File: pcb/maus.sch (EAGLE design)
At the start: 84 parts, among them IC1 AD712R, Q2 BSS123, Q3 BSL307SP, Q4 BSS123, T1 BC847, T2 BC847, U1 ESP32-S2-WROOM, U2 CH340C, U3 CP2102, U4 LP3965EMP-3.3, U5 LSM9DS1TR

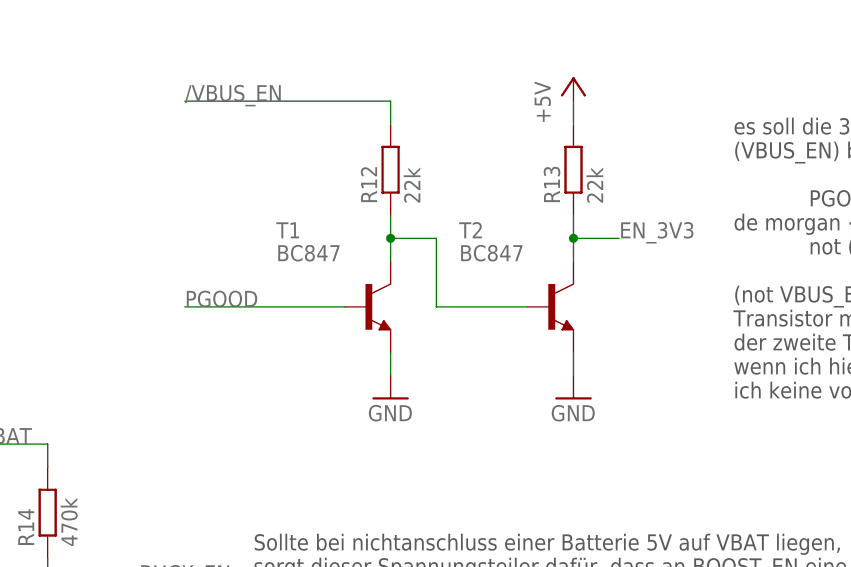
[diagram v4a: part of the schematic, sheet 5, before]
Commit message: swapped BC847 -> BSS123 in power schematics
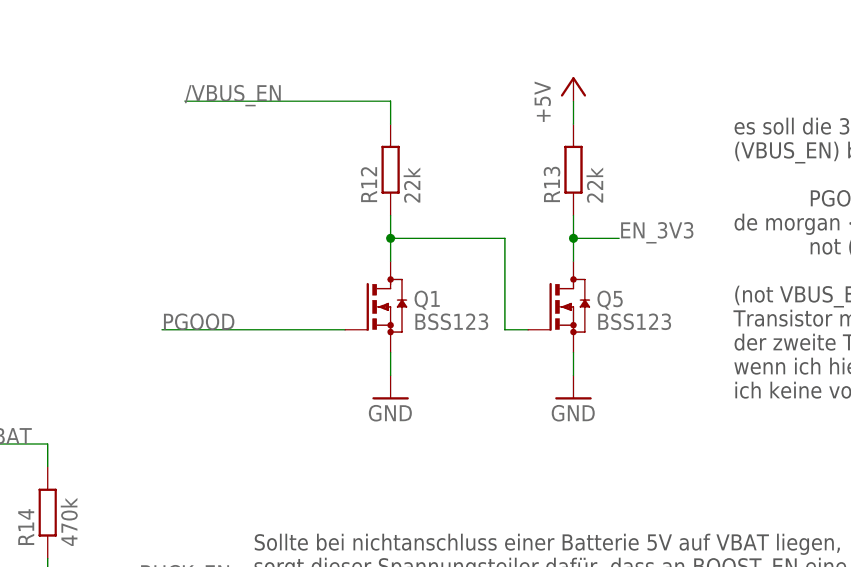
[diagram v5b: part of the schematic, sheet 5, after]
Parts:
- removed T1, T2: BC847, transistor:BC847
- added Q1, Q5: BSS123, transistor-small-signal:BSS123
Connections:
- net EN_3V3: now also Q5.D; no longer T2.C
- net GND: now also Q1.S, Q5.S; no longer T1.E, T2.E
- net N$20: now also Q1.D, Q5.G; no longer T1.C, T2.B
- net PGOOD: now also Q1.G; no longer T1.B
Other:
- note added: "Auto program table ---------------- DTR RTS EN IO0 --------------- |1 |1 | 1 | 1 |0 |0 | 1 | 1 |1 |0 | 0 | 1 |0 |1 | 1 | 0"
- note removed: "Auto program table ---------------- DTR RTS EN IO0 --------------- |1 |1 | 1 | 1 |0 |0 | 1 | 1 |1 |0 | 0 | 0 |0 |1 | 1 | 0"
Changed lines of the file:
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@@
 <part name="GND11" library="supply1" library_urn="urn:adsk.eagle:library:371" deviceset="GND" device=""/>
 <part name="P+5" library="supply1" library_urn="urn:adsk.eagle:library:371" deviceset="+5V" device=""/>
-<part name="T1" library="transistor" library_urn="urn:adsk.eagle:library:402" deviceset="BC847" device="" package3d_urn="urn:adsk.eagle:package:28738/2"/>
 <part name="R12" library="rcl" library_urn="urn:adsk.eagle:library:334" deviceset="R-EU_" device="R0603" package3d_urn="urn:adsk.eagle:package:23555/3" value="22k"/>
 <part name="GND12" library="supply1" library_urn="urn:adsk.eagle:library:371" deviceset="GND" device=""/>
 <part name="P+6" library="supply1" library_urn="urn:adsk.eagle:library:371" deviceset="+5V" device=""/>
-<part name="T2" library="transistor" library_urn="urn:adsk.eagle:library:402" deviceset="BC847" device="" package3d_urn="urn:adsk.eagle:package:28738/2"/>
 <part name="R13" library="rcl" library_urn="urn:adsk.eagle:library:334" deviceset="R-EU_" device="R0603" package3d_urn="urn:adsk.eagle:package:23555/3" value="22k"/>
 <part name="GND13" library="supply1" library_urn="urn:adsk.eagle:library:371" deviceset="GND" device=""/>
@@
 <part name="P+8" library="supply1" library_urn="urn:adsk.eagle:library:371" deviceset="+5V" device=""/>
 <part name="P+9" library="supply1" library_urn="urn:adsk.eagle:library:371" deviceset="+5V" device=""/>
+<part name="Q1" library="transistor-small-signal" library_urn="urn:adsk.eagle:library:401" deviceset="BSS123" device="" package3d_urn="urn:adsk.eagle:package:28738/2"/>
+<part name="Q5" library="transistor-small-signal" library_urn="urn:adsk.eagle:library:401" deviceset="BSS123" device="" package3d_urn="urn:adsk.eagle:package:28738/2"/>
 </parts>
 <sheets>
@@
 |1     |1      | 1   | 1
 |0     |0      | 1   | 1
-|1     |0      | 0   | 0
+|1     |0      | 0   | 1
 |0     |1      | 1   | 0 </text>
 <text x="276.86" y="63.5" size="1.778" layer="97">UART0 Activity LEDs</text>
@@
 <attribute name="VALUE" x="139.7" y="58.42" size="1.778" layer="96" rot="R90"/>
 </instance>
-<instance part="T1" gate="G$1" x="210.82" y="60.96" smashed="yes">
-<attribute name="NAME" x="200.66" y="68.58" size="1.778" layer="95"/>
-<attribute name="VALUE" x="200.66" y="66.04" size="1.778" layer="96"/>
-</instance>
 <instance part="R12" gate="G$1" x="213.36" y="76.2" smashed="yes" rot="R90">
 <attribute name="NAME" x="211.8614" y="72.39" size="1.778" layer="95" rot="R90"/>
@@
 <attribute name="VALUE" x="231.14" y="81.28" size="1.778" layer="96" rot="R90"/>
 </instance>
-<instance part="T2" gate="G$1" x="231.14" y="60.96" smashed="yes">
-<attribute name="NAME" x="220.98" y="68.58" size="1.778" layer="95"/>
-<attribute name="VALUE" x="220.98" y="66.04" size="1.778" layer="96"/>
-</instance>
 <instance part="R13" gate="G$1" x="233.68" y="76.2" smashed="yes" rot="R90">
 <attribute name="NAME" x="232.1814" y="72.39" size="1.778" layer="95" rot="R90"/>
@@
 <instance part="GND16" gate="1" x="17.78" y="81.28" smashed="yes">
 <attribute name="VALUE" x="15.24" y="78.74" size="1.778" layer="96"/>
+</instance>
+<instance part="Q1" gate="G$1" x="213.36" y="60.96" smashed="yes">
+<attribute name="NAME" x="215.9" y="60.96" size="1.778" layer="95"/>
+<attribute name="VALUE" x="215.9" y="58.42" size="1.778" layer="96"/>
+</instance>
+<instance part="Q5" gate="G$1" x="233.68" y="60.96" smashed="yes">
+<attribute name="NAME" x="236.22" y="60.96" size="1.778" layer="95"/>
+<attribute name="VALUE" x="236.22" y="58.42" size="1.778" layer="96"/>
 </instance>
 </instances>
@@
 </segment>
 <segment>
-<pinref part="T1" gate="G$1" pin="E"/>
 <pinref part="GND12" gate="1" pin="GND"/>
 <wire x1="213.36" y1="55.88" x2="213.36" y2="53.34" width="0.1524" layer="91"/>
-</segment>
-<segment>
-<pinref part="T2" gate="G$1" pin="E"/>
+<pinref part="Q1" gate="G$1" pin="S"/>
+</segment>
+<segment>
 <pinref part="GND13" gate="1" pin="GND"/>
 <wire x1="233.68" y1="55.88" x2="233.68" y2="53.34" width="0.1524" layer="91"/>
+<pinref part="Q5" gate="G$1" pin="S"/>
 </segment>
 <segment>
@@
 </segment>
 <segment>
-<pinref part="T1" gate="G$1" pin="B"/>
-<wire x1="208.28" y1="60.96" x2="190.5" y2="60.96" width="0.1524" layer="91"/>
-<label x="190.5" y="60.96" size="1.778" layer="95"/>
+<wire x1="208.28" y1="58.42" x2="187.96" y2="58.42" width="0.1524" layer="91"/>
+<label x="187.96" y="58.42" size="1.778" layer="95"/>
+<pinref part="Q1" gate="G$1" pin="G"/>
 </segment>
 </net>
@@
 <segment>
 <pinref part="R13" gate="G$1" pin="1"/>
-<pinref part="T2" gate="G$1" pin="C"/>
 <wire x1="233.68" y1="71.12" x2="233.68" y2="68.58" width="0.1524" layer="91"/>
 <wire x1="233.68" y1="68.58" x2="233.68" y2="66.04" width="0.1524" layer="91"/>
@@
 <junction x="233.68" y="68.58"/>
 <label x="238.76" y="68.58" size="1.778" layer="95"/>
+<pinref part="Q5" gate="G$1" pin="D"/>
 </segment>
 </net>
@@
 <segment>
 <pinref part="R12" gate="G$1" pin="1"/>
-<pinref part="T1" gate="G$1" pin="C"/>
 <wire x1="213.36" y1="71.12" x2="213.36" y2="68.58" width="0.1524" layer="91"/>
 <wire x1="213.36" y1="68.58" x2="213.36" y2="66.04" width="0.1524" layer="91"/>
-<wire x1="213.36" y1="68.58" x2="218.44" y2="68.58" width="0.1524" layer="91"/>
 <junction x="213.36" y="68.58"/>
-<wire x1="218.44" y1="68.58" x2="218.44" y2="60.96" width="0.1524" layer="91"/>
-<pinref part="T2" gate="G$1" pin="B"/>
-<wire x1="218.44" y1="60.96" x2="228.6" y2="60.96" width="0.1524" layer="91"/>
-</segment>
-</net>
+<pinref part="Q1" gate="G$1" pin="D"/>
+<wire x1="213.36" y1="68.58" x2="226.06" y2="68.58" width="0.1524" layer="91"/>
+<wire x1="226.06" y1="68.58" x2="226.06" y2="58.42" width="0.1524" layer="91"/>
+<pinref part="Q5" gate="G$1" pin="G"/>
+<wire x1="226.06" y1="58.42" x2="228.6" y2="58.42" width="0.1524" layer="91"/>
+</segment>
+</net>

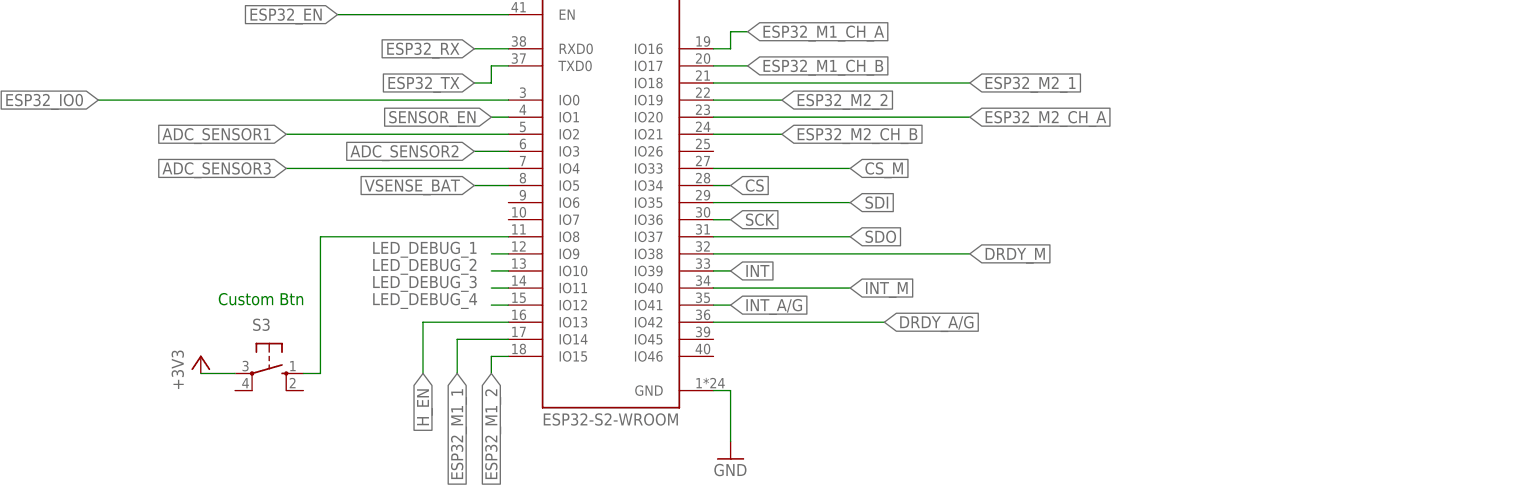
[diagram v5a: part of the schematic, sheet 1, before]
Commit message: pinheader forleftover pins, new sensor naming
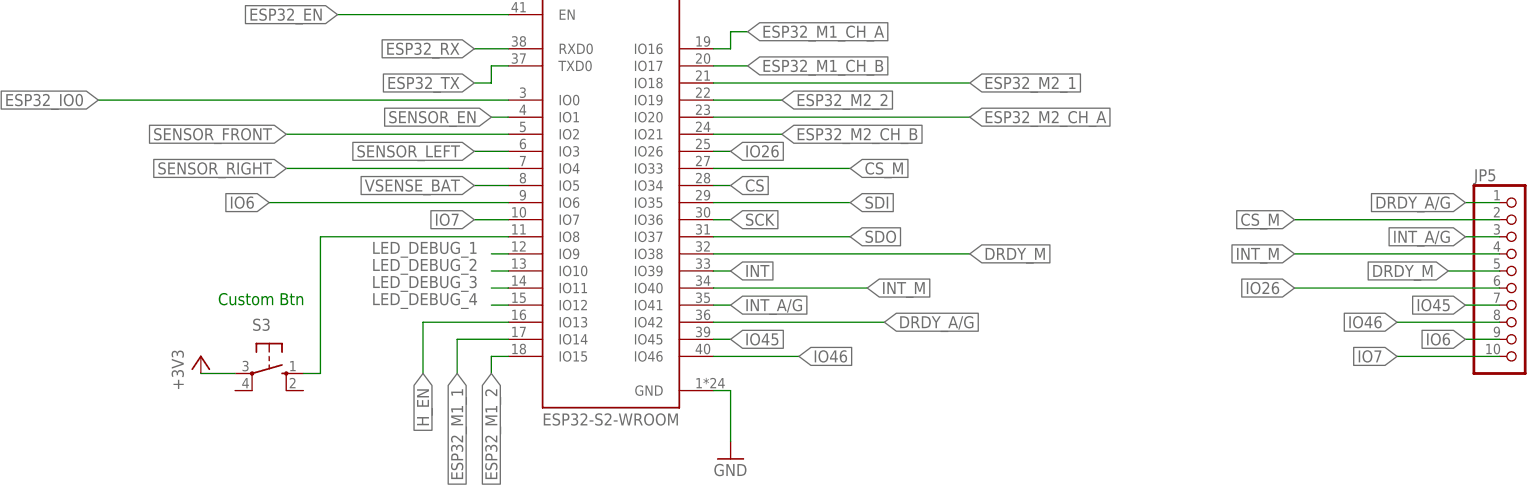
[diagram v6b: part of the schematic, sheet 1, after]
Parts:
- added JP5: (no value), pinhead:PINHD-1X10
- renumbered JP1 to SENSOR_FRONT, JP2 to SENSOR_LEFT, JP3 to SENSOR_RIGHT
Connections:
- net ADC_SENSOR1 renamed SENSOR_FRONT
- net ADC_SENSOR2 renamed SENSOR_LEFT
- net ADC_SENSOR3 renamed SENSOR_RIGHT
- new net IO26: JP5.6, U1.IO26
- new net IO45: JP5.7, U1.IO45
- new net IO46: JP5.8, U1.IO46
- new net IO6: JP5.9, U1.IO6
- new net IO7: JP5.10, U1.IO7
- net CS_M: now also JP5.2
- net DRDY_A/G: now also JP5.1
- net DRDY_M: now also JP5.5
- net INT_A/G: now also JP5.3
- net INT_M: now also JP5.4

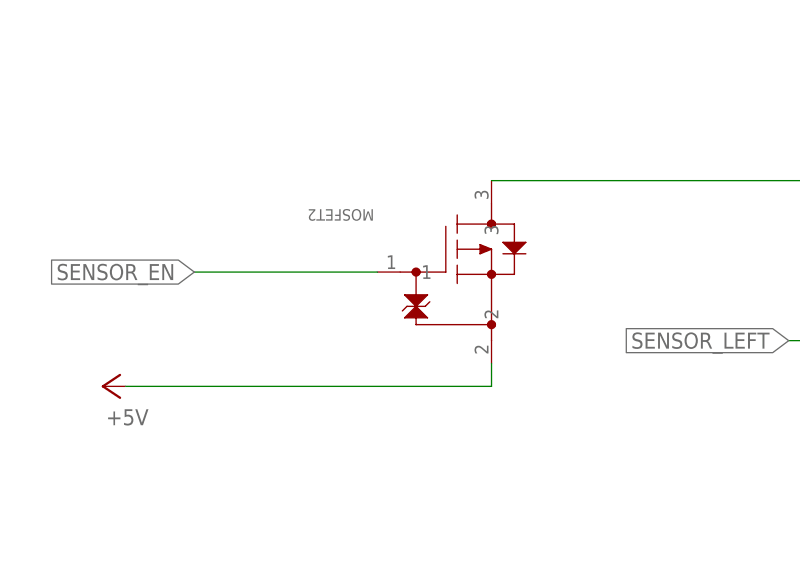
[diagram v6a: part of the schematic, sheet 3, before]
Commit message: replaced pmos fets in schematic with the new one
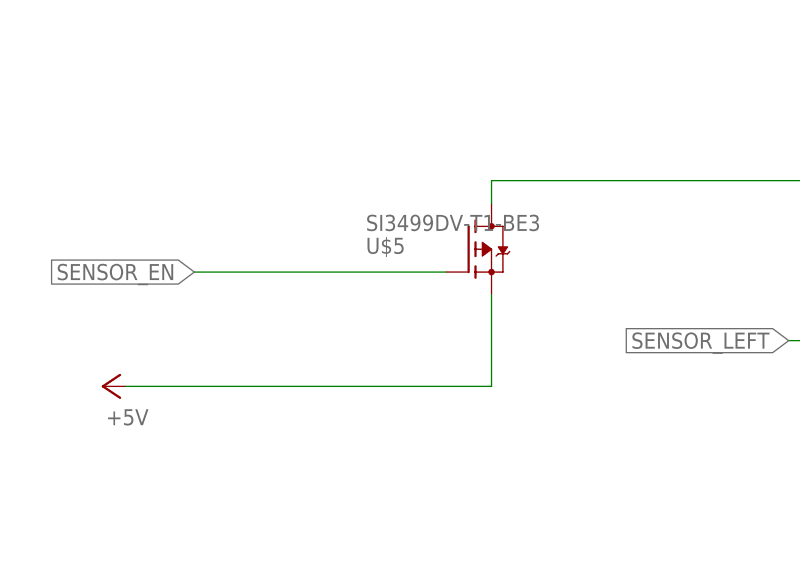
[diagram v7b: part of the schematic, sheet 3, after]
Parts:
- removed MOSFET2: SSM3J117TU(TE85L), SSM3J117TU:SSM3J117TU(TE85L)
- removed Q3: BSL307SP, transistor-fet:BSL307SP
- added U$5, U$6: SI3499DV-T1-BE3, mosfet:SI3499DV-T1-BE3
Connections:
- net +5V: now also U$5.S, U$6.S; no longer MOSFET2.2, Q3.S
- net /VBUS_EN: now also U$6.G; no longer Q3.G
- net N$7: now also U$5.D; no longer MOSFET2.3
- net SENSOR_EN: now also U$5.G; no longer MOSFET2.1
- net USB_VBUS: now also U$6.D; no longer Q3.D
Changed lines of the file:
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@@
 <part name="GND1" library="supply1" library_urn="urn:adsk.eagle:library:371" deviceset="GND" device=""/>
 <part name="C1" library="rcl" library_urn="urn:adsk.eagle:library:334" deviceset="C-EU" device="C0805" package3d_urn="urn:adsk.eagle:package:23617/2" value="10uF"/>
-<part name="MOSFET2" library="SSM3J117TU" deviceset="SSM3J117TU(TE85L)" device=""/>
 <part name="C6" library="rcl" library_urn="urn:adsk.eagle:library:334" deviceset="C-EU" device="C0805" package3d_urn="urn:adsk.eagle:package:23617/2" value="10uF"/>
 <part name="C7" library="rcl" library_urn="urn:adsk.eagle:library:334" deviceset="C-EU" device="C0805" package3d_urn="urn:adsk.eagle:package:23617/2" value="10uF"/>
@@
 <part name="IC1" library="analog-devices" library_urn="urn:adsk.eagle:library:102" deviceset="AD712" device="R" package3d_urn="urn:adsk.eagle:package:30987/2"/>
 <part name="P+2" library="supply1" library_urn="urn:adsk.eagle:library:371" deviceset="+5V" device=""/>
-<part name="Q3" library="transistor-fet" library_urn="urn:adsk.eagle:library:396" deviceset="BSL307SP" device="" package3d_urn="urn:adsk.eagle:package:28543/2"/>
 <part name="P+3" library="supply1" library_urn="urn:adsk.eagle:library:371" deviceset="+5V" device=""/>
 <part name="+3V2" library="supply1" library_urn="urn:adsk.eagle:library:371" deviceset="+3V3" device=""/>
@@
 <part name="Q5" library="transistor-small-signal" library_urn="urn:adsk.eagle:library:401" deviceset="BSS123" device="" package3d_urn="urn:adsk.eagle:package:28738/2"/>
 <part name="JP5" library="pinhead" library_urn="urn:adsk.eagle:library:325" deviceset="PINHD-1X10" device="" package3d_urn="urn:adsk.eagle:package:22406/2"/>
+<part name="U$5" library="mosfet" deviceset="SI3499DV-T1-BE3" device="" package3d_urn="urn:adsk.eagle:package:33743404/1"/>
+<part name="U$6" library="mosfet" deviceset="SI3499DV-T1-BE3" device="" package3d_urn="urn:adsk.eagle:package:33743404/1"/>
 </parts>
 <sheets>
@@
 <attribute name="VALUE" x="153.924" y="101.981" size="1.778" layer="96"/>
 </instance>
-<instance part="MOSFET2" gate="A" x="55.88" y="96.52" smashed="yes">
-<attribute name="NAME" x="53.0098" y="95.885" size="1.27" layer="95" ratio="6" rot="SR180"/>
-</instance>
 <instance part="C6" gate="G$1" x="152.4" y="66.04" smashed="yes">
 <attribute name="NAME" x="153.924" y="66.421" size="1.778" layer="95"/>
@@
 <instance part="P+1" gate="1" x="22.86" y="76.2" smashed="yes" rot="R90">
 <attribute name="VALUE" x="27.94" y="73.66" size="1.778" layer="96" rot="R180"/>
+</instance>
+<instance part="U$5" gate="T$1" x="63.5" y="91.44" smashed="yes" rot="MR180">
+<attribute name="VALUE" x="52.07" y="95.25" size="1.778" layer="96" rot="MR180"/>
+<attribute name="NAME" x="52.07" y="92.71" size="1.778" layer="95" rot="MR180"/>
 </instance>
 </instances>
@@
 <wire x1="165.1" y1="58.42" x2="165.1" y2="66.04" width="0.1524" layer="91"/>
 <wire x1="165.1" y1="66.04" x2="182.88" y2="66.04" width="0.1524" layer="91"/>
-<pinref part="MOSFET2" gate="A" pin="3"/>
+<pinref part="U$5" gate="T$1" pin="D"/>
+<wire x1="66.04" y1="96.52" x2="66.04" y2="99.06" width="0.1524" layer="91"/>
 </segment>
 </net>
@@
 <net name="SENSOR_EN" class="0">
 <segment>
-<pinref part="MOSFET2" gate="A" pin="1"/>
-<wire x1="53.34" y1="88.9" x2="33.02" y2="88.9" width="0.1524" layer="91"/>
+<wire x1="60.96" y1="88.9" x2="33.02" y2="88.9" width="0.1524" layer="91"/>
 <label x="33.02" y="88.9" size="1.778" layer="95" rot="R180" xref="yes"/>
+<pinref part="U$5" gate="T$1" pin="G"/>
 </segment>
 </net>
 <net name="+5V" class="0">
 <segment>
-<pinref part="MOSFET2" gate="A" pin="2"/>
 <wire x1="25.4" y1="76.2" x2="66.04" y2="76.2" width="0.1524" layer="91"/>
-<wire x1="66.04" y1="76.2" x2="66.04" y2="78.74" width="0.1524" layer="91"/>
 <pinref part="P+1" gate="1" pin="+5V"/>
+<pinref part="U$5" gate="T$1" pin="S"/>
+<wire x1="66.04" y1="86.36" x2="66.04" y2="76.2" width="0.1524" layer="91"/>
 </segment>
 </net>
@@
 <attribute name="VALUE" x="27.94" y="137.16" size="1.778" layer="96" rot="R90"/>
 </instance>
-<instance part="Q3" gate="G$1" x="96.52" y="96.52" smashed="yes" rot="R270">
-<attribute name="VALUE" x="92.71" y="107.95" size="1.778" layer="96" rot="R270"/>
-<attribute name="NAME" x="95.25" y="107.95" size="1.778" layer="95" rot="R270"/>
-</instance>
 <instance part="P+3" gate="1" x="111.76" y="99.06" smashed="yes">
 <attribute name="VALUE" x="109.22" y="93.98" size="1.778" layer="96" rot="R90"/>
@@
 <attribute name="NAME" x="236.22" y="60.96" size="1.778" layer="95"/>
 <attribute name="VALUE" x="236.22" y="58.42" size="1.778" layer="96"/>
+</instance>
+<instance part="U$6" gate="T$1" x="96.52" y="96.52" smashed="yes" rot="R270">
+<attribute name="VALUE" x="92.71" y="107.95" size="1.778" layer="96" rot="R270"/>
+<attribute name="NAME" x="95.25" y="107.95" size="1.778" layer="95" rot="R270"/>
 </instance>
 </instances>
@@
 </segment>
 <segment>
-<pinref part="Q3" gate="G$1" pin="S"/>
 <pinref part="P+3" gate="1" pin="+5V"/>
 <wire x1="101.6" y1="93.98" x2="111.76" y2="93.98" width="0.1524" layer="91"/>
 <wire x1="111.76" y1="93.98" x2="111.76" y2="96.52" width="0.1524" layer="91"/>
+<pinref part="U$6" gate="T$1" pin="S"/>
 </segment>
 <segment>
@@
 <segment>
 <pinref part="IC1" gate="A" pin="OUT"/>
-<pinref part="Q3" gate="G$1" pin="G"/>
 <wire x1="83.82" y1="119.38" x2="99.06" y2="119.38" width="0.1524" layer="91"/>
 <wire x1="99.06" y1="119.38" x2="99.06" y2="99.06" width="0.1524" layer="91"/>
 <label x="88.9" y="119.38" size="1.778" layer="95"/>
+<pinref part="U$6" gate="T$1" pin="G"/>
 </segment>
 <segment>
@@
 <net name="USB_VBUS" class="0">
 <segment>
-<pinref part="Q3" gate="G$1" pin="D"/>
 <wire x1="91.44" y1="93.98" x2="66.04" y2="93.98" width="0.1524" layer="91"/>
 <label x="66.04" y="93.98" size="1.778" layer="95"/>
-</segment>
-</net>
+<pinref part="U$6" gate="T$1" pin="D"/>
+</segment>
+</net>
